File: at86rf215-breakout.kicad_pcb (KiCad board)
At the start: 2 copper layers, 30.5 x 35.8 mm, 36 parts, among them J1 RPi Header, U1 AT86RF215-ZU

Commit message: Update to v0.1
- Use SMD instead for thru-hole pin header for lower assembly cost
- Place pin header on top side, so that only one side needs SMD assembly
- Move pin header to allow placement on MIoT-Lab Testbed Nodes
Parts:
- added G***: LOGO, local:ComSys-Logo-Big, B.Cu at (28.1, 31.4)
- J1: footprint Connector_PinSocket_2.54mm:PinSocket_2x06_P2.54mm_Vertical -> Connector_PinSocket_2.54mm:PinSocket_2x06_P2.54mm_Vertical_SMD; moved to F.Cu
- RF24: value ANT -> Antenna
- moved C11 2.50 mm to (22.6, 36.6)
- moved J1 2.00 mm to (17.2, 38.7)
- moved C10 0.61 mm to (24.1, 36.0)
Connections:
- B1 pad 6: (no net) -> Net-(B1-Pad6)
- J1 pad 1: (no net) -> Net-(J1-Pad1)
- J1 pad 12: (no net) -> Net-(J1-Pad12)
- J1 pad 8: (no net) -> Net-(J1-Pad8)
- U1 pad 1: (no net) -> Net-(U1-Pad1)
- U1 pad 11: (no net) -> Net-(U1-Pad11)
- U1 pad 12: (no net) -> Net-(U1-Pad12)
- U1 pad 2: (no net) -> Net-(U1-Pad2)
- U1 pad 22: (no net) -> Net-(U1-Pad22)
- U1 pad 25: (no net) -> Net-(U1-Pad25)
- U1 pad 26: (no net) -> Net-(U1-Pad26)
- U1 pad 27: (no net) -> Net-(U1-Pad27)
- U1 pad 28: (no net) -> Net-(U1-Pad28)
- U1 pad 30: (no net) -> Net-(U1-Pad30)
- U1 pad 31: (no net) -> Net-(U1-Pad31)
- U1 pad 33: (no net) -> Net-(U1-Pad33)
- U1 pad 34: (no net) -> Net-(U1-Pad34)
- U1 pad 35: (no net) -> Net-(U1-Pad35)
- U1 pad 36: (no net) -> Net-(U1-Pad36)
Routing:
- net /MISO: track 28.9 -> 12.3 mm, vias 0 -> 2
- net /MOSI: track 20.4 -> 11.4 mm, vias 0 -> 2
- net /RST: track 26.8 -> 18.6 mm, vias 3 -> 2
- net /SCLK: track 19.3 -> 12.1 mm
- net /IRQ: track 13.5 -> 19.4 mm, vias 1 -> 0
- net /SEL: track 22.7 -> 18.8 mm
- net VDD: track 53.5 -> 51.5 mm, vias 6 -> 7
- net GND: vias 36 -> 38
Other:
- board text added: "IEEE 802.15.4g-2012 Transceiver Dual Band (868 MHz & 2.4 GHz)"
- board text added: "J1"
- board text added: "v0.1"
- board text removed: "IEEE 802.15.4g-2012 Transceiver Dual Band (868/900 MHz & 2.4 GHz)"
- board text removed: "v0.0"

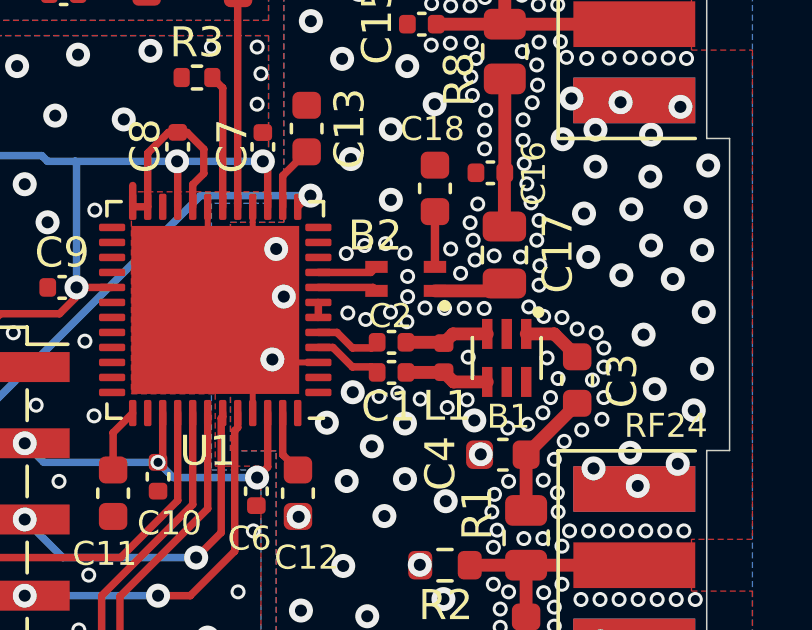
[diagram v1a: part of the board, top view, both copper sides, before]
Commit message: Use same baluns as AT86RF215-XPRO
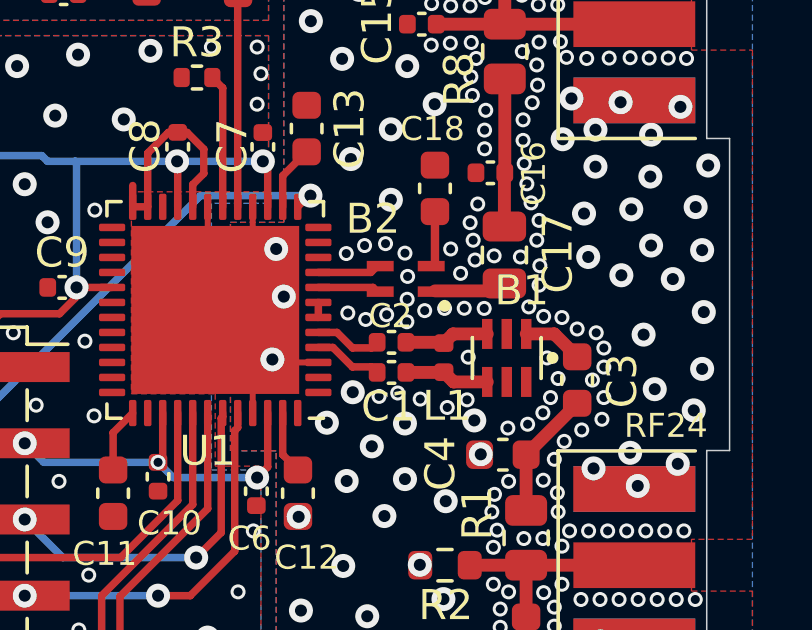
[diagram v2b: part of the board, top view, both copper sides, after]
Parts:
- B1: footprint local:TDK-HHM1711D1 -> local:2450FB15A050
- B2: value ATB2012-75011-T000 -> DLW21SN900SQ2L; footprint local:ATB2012-75011-T000 -> local:DLW21SN900SQ2L
- turned B1 to 0 degrees
- turned B2 to 0 degrees

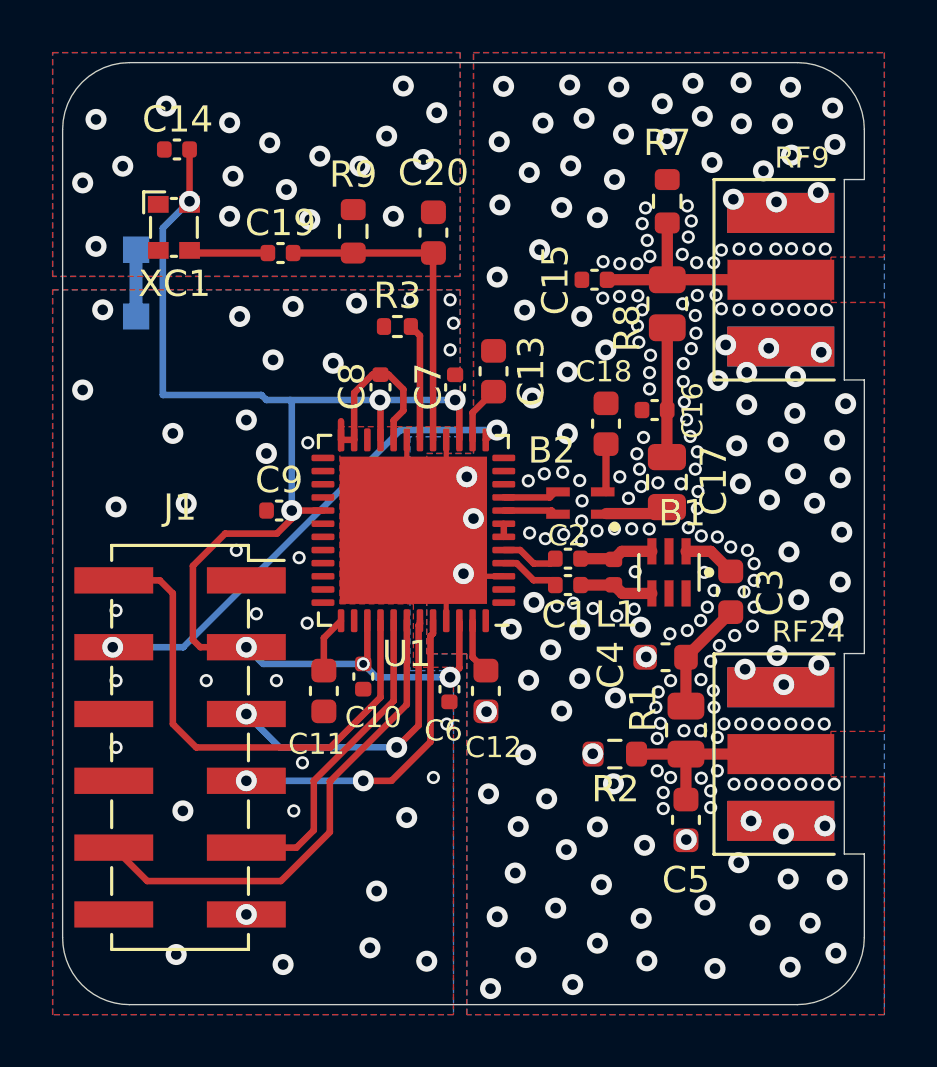
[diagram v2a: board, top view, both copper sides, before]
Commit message: Added test points
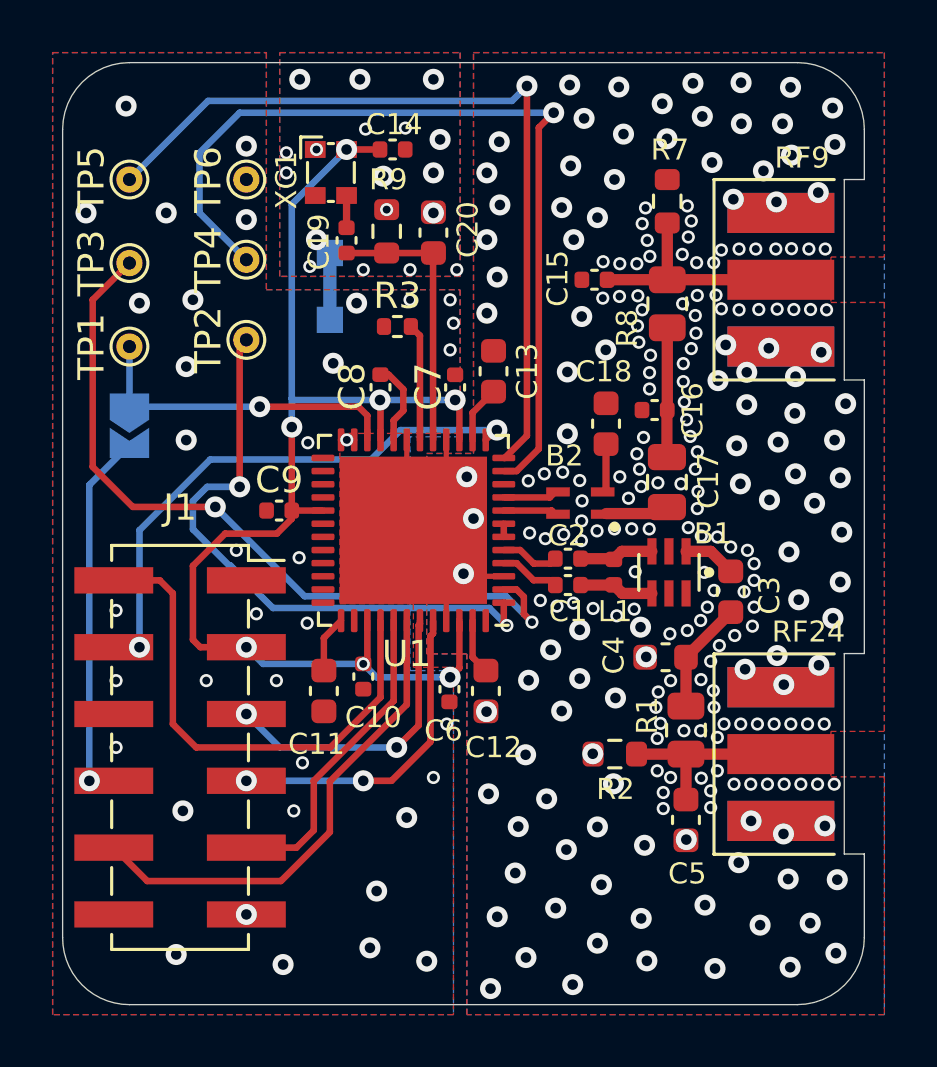
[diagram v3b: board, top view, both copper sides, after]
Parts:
- added JP1: solder jumper, Jumper:SolderJumper-2_P1.3mm_Open_TrianglePad1.0x1.5mm, B.Cu at (15.2, 26.5)
- added TP1: CLKO, TestPoint:TestPoint_THTPad_D1.0mm_Drill0.5mm, F.Cu at (15.2, 23.5)
- added TP2: FEA24, TestPoint:TestPoint_THTPad_D1.0mm_Drill0.5mm, F.Cu at (19.7, 23.2)
- added TP3: FEB24, TestPoint:TestPoint_THTPad_D1.0mm_Drill0.5mm, F.Cu at (15.2, 20.3)
- added TP4: FEA09, TestPoint:TestPoint_THTPad_D1.0mm_Drill0.5mm, F.Cu at (19.7, 20.2)
- added TP5: FEB09, TestPoint:TestPoint_THTPad_D1.0mm_Drill0.5mm, F.Cu at (15.2, 17.1)
- added TP6: GND, TestPoint:TestPoint_THTPad_D1.0mm_Drill0.5mm, F.Cu at (19.7, 17.1)
- B1: value Balun_HHM1711D1 -> Balun 2.4 GHz
- B2: value DLW21SN900SQ2L -> Balun 868 MHz
- moved C14 8.20 mm to (25.2, 16.0), turned to 0 degrees
- moved R4 7.37 mm to (22.9, 21.2)
- moved XC1 6.32 mm to (22.9, 16.9)
- moved C19 2.56 mm to (23.5, 19.5), turned to 90 degrees
- moved R9 1.27 mm to (25.0, 19.1)
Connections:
- J1 pad 8: Net-(J1-Pad8) -> /CLKO'
- U1 pad 1: Net-(U1-Pad1) -> /FEA24
- U1 pad 11: Net-(U1-Pad11) -> /FEA09
- U1 pad 12: Net-(U1-Pad12) -> /FEB09
- U1 pad 2: Net-(U1-Pad2) -> /FEB24
- U1 pad 22: Net-(U1-Pad22) -> /CLKO
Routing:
- net /FEA09: track 0.00 -> 33.6 mm, vias 0 -> 1
- net /FEB09: track 0.00 -> 31.1 mm, vias 0 -> 1
- net /FEB24: track 0.00 -> 29.4 mm, vias 0 -> 2
- net /FEA24: track 0.00 -> 23.1 mm, vias 0 -> 2
- net /CLKO': track 0.00 -> 13.4 mm, vias 0 -> 1
- net /CLKO: track 0.00 -> 12.4 mm, vias 0 -> 1
- net GND: track 7.46 -> 3.68 mm
- net VDD: track 51.5 -> 48.4 mm
- net /TCXO: track 12.4 -> 10.4 mm
- net /TCXO': track 2.98 -> 1.23 mm
- net /RST: track 18.6 -> 20.2 mm
- net GNDA: track 16.3 -> 16.1 mm, vias 240 -> 237
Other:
- board text added: "A09"
- board text added: "A24"
- board text added: "B09"
- board text added: "B24"
- board text added: "CLKO"
- board text added: "IEEE 802.15.4g-2012 Transceiver 868 MHz & 2.4 GHz"
- board text removed: "IEEE 802.15.4g-2012 Transceiver Dual Band (868 MHz & 2.4 GHz)"

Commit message: Use different TCXO
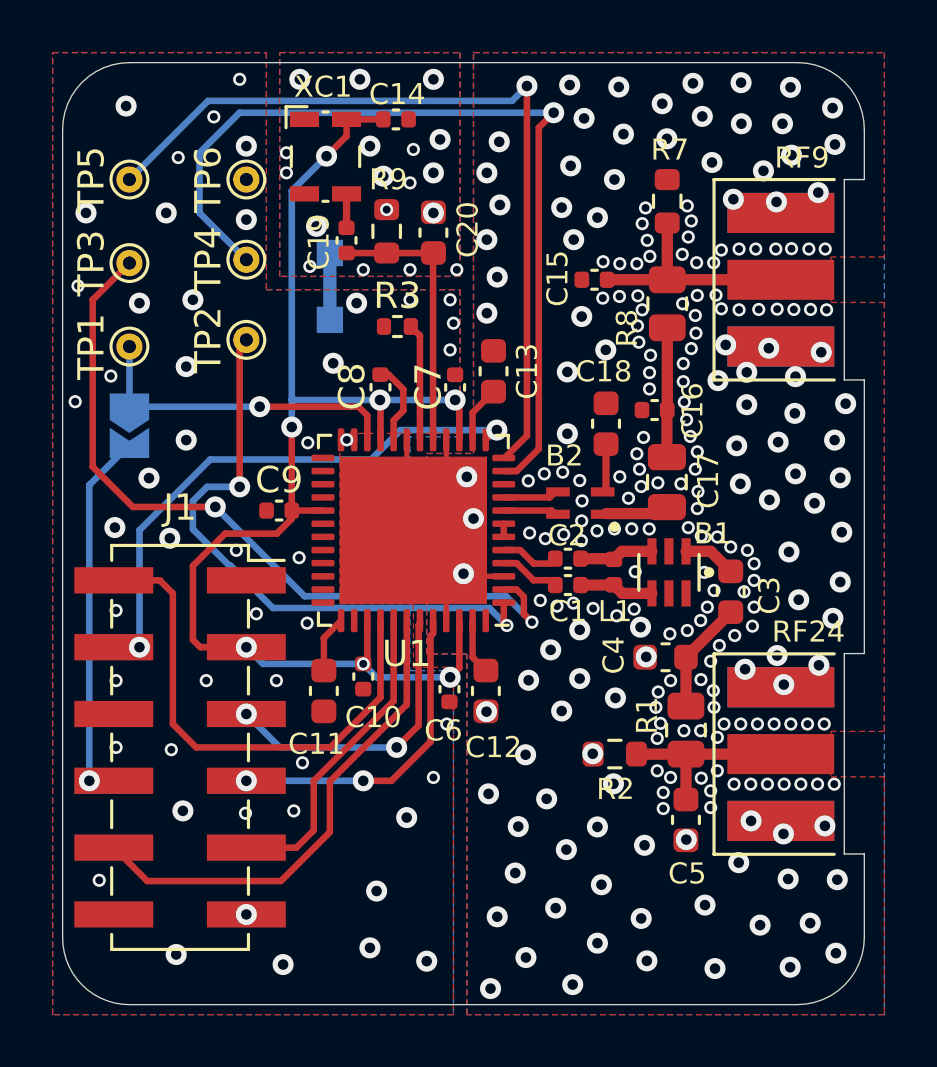
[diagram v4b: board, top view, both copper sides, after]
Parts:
- XC1: value TXC_7Z26001013 -> 26 MHz TCXO; footprint local:TXC_7Z26001013 -> local:QTT325-26_000MBN-T
- moved C14 1.15 mm to (25.4, 14.9)
- moved XC1 0.64 mm to (22.7, 16.3)
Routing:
- net VDD: track 48.4 -> 49.6 mm
- net GND: vias 38 -> 50

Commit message: Change used TCXO
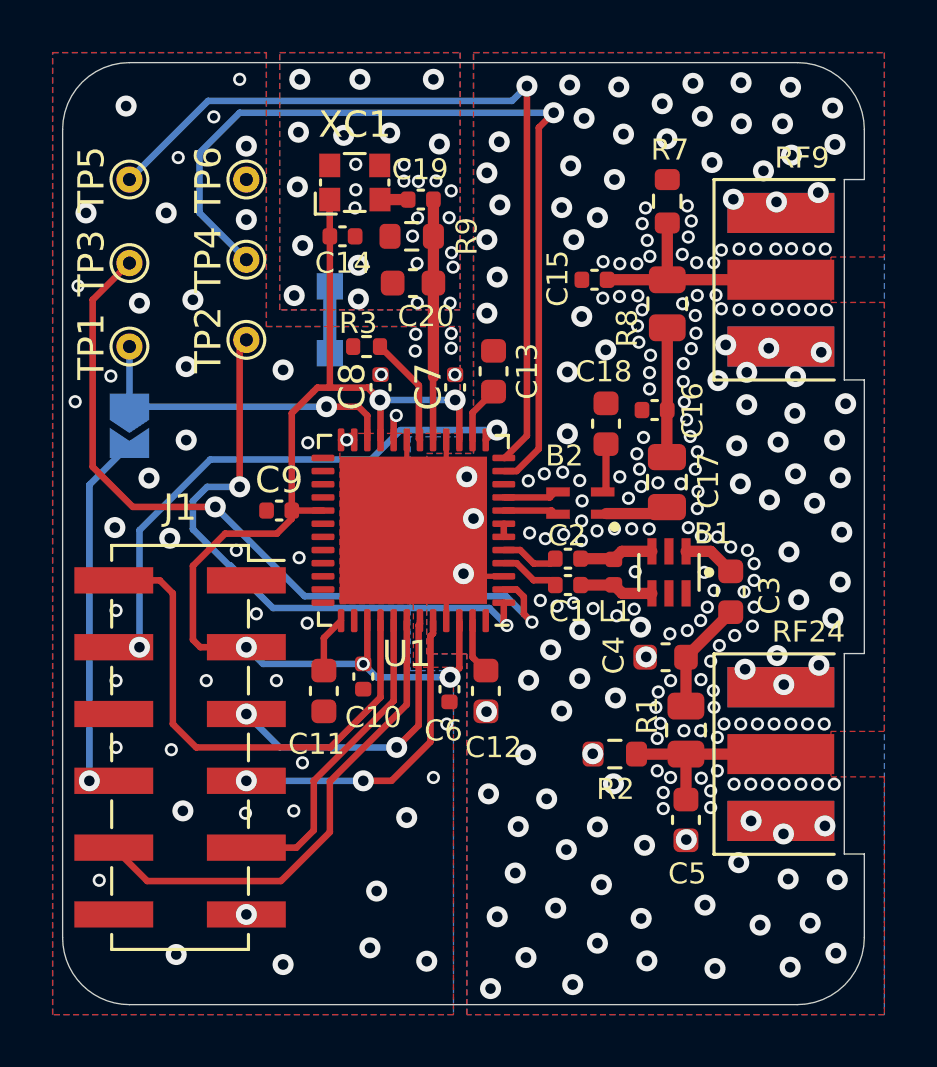
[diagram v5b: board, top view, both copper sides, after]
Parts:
- XC1: footprint local:QTT325-26_000MBN-T -> local:IQD_LFTCXO078374REEL
- moved C14 4.89 mm to (23.3, 19.3)
- moved C19 3.22 mm to (26.3, 17.9), turned to 180 degrees
- moved C20 2.07 mm to (26.0, 21.1), turned to 180 degrees
- moved XC1 1.48 mm to (23.8, 17.3), turned to 0 degrees
- moved R3 1.40 mm to (24.3, 23.5)
- moved R4 1.27 mm to (22.9, 22.5)
- moved R9 0.97 mm to (26.0, 19.3), turned to 180 degrees
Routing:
- net VDD: track 49.6 -> 44.0 mm, vias 7 -> 5
- net GND: track 3.68 -> 1.47 mm, vias 50 -> 52
- net /TCXO: track 10.4 -> 9.12 mm
- net GND2: vias 18 -> 28

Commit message: Fixed footprint of TCXO
Datasheet is in bottom view, not top view :-/
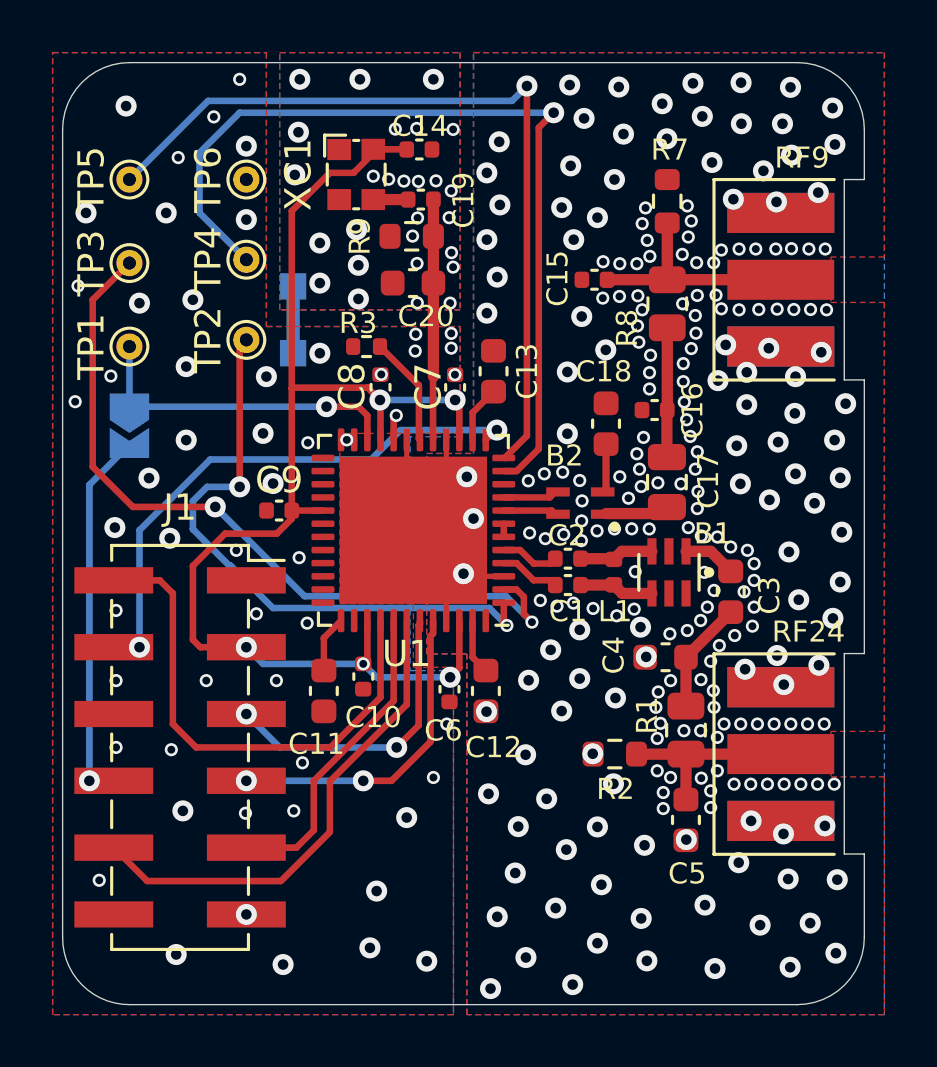
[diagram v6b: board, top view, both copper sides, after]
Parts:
- moved C14 4.41 mm to (26.3, 16.0)
- moved R4 1.40 mm to (21.5, 22.5)
- moved XC1 0.31 mm to (23.9, 17.0), turned to 90 degrees
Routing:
- net VDD: track 44.0 -> 49.5 mm
- net GND2: vias 28 -> 27
- net GND: vias 52 -> 55
